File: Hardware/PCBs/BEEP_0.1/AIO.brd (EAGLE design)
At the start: 110 x 110 mm, 89 parts, among them IC1 ULN2803ASOP18, IC2 ULN2803ASOP18, U1 ATXMEGA64D3-AU, U2 TB6612FNG

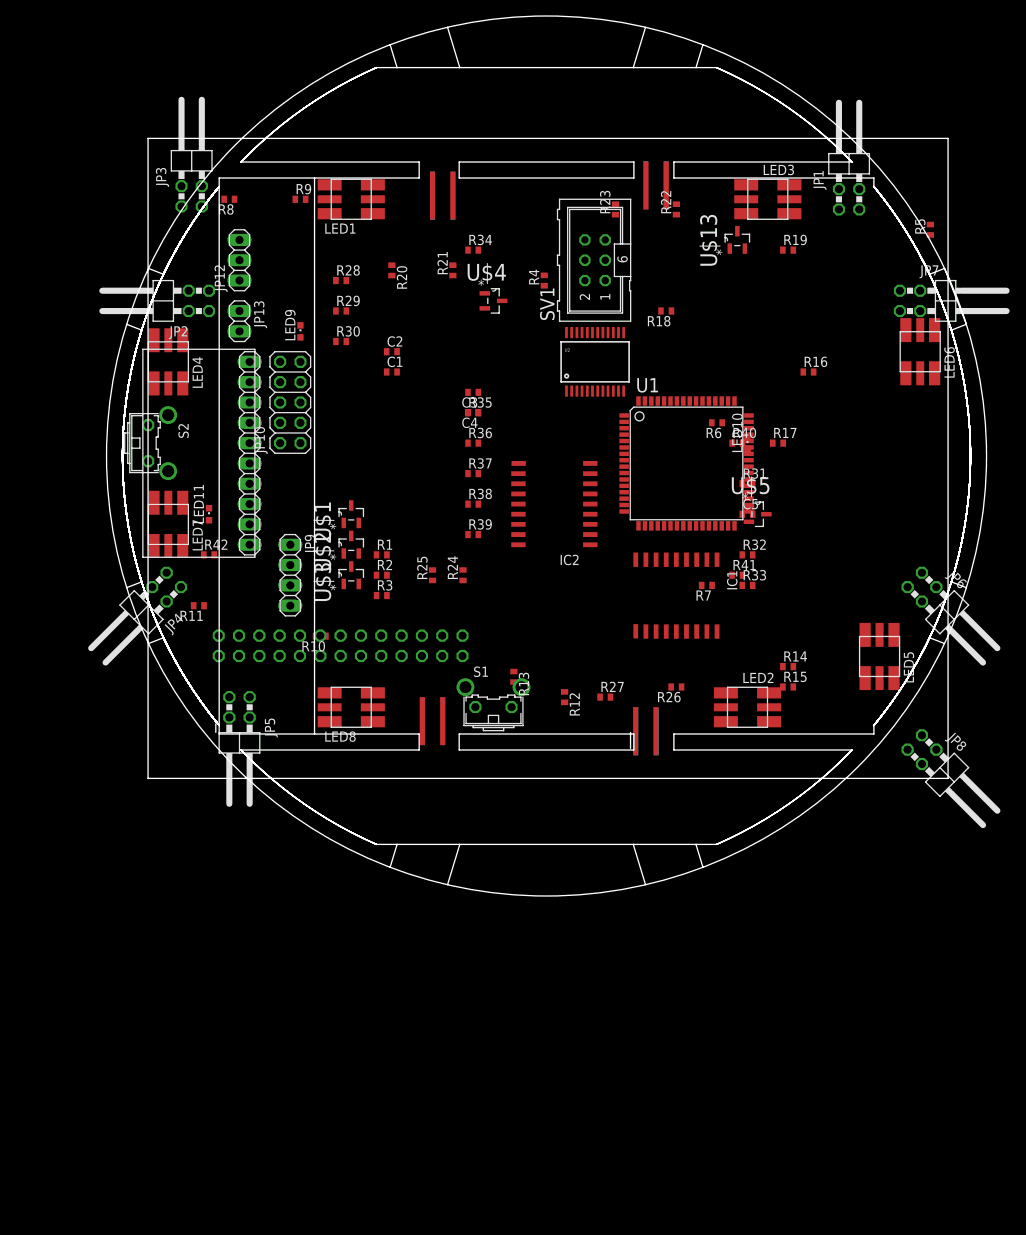
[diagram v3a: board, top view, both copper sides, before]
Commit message: enhance BEEP main pcb, rgb and ir boards
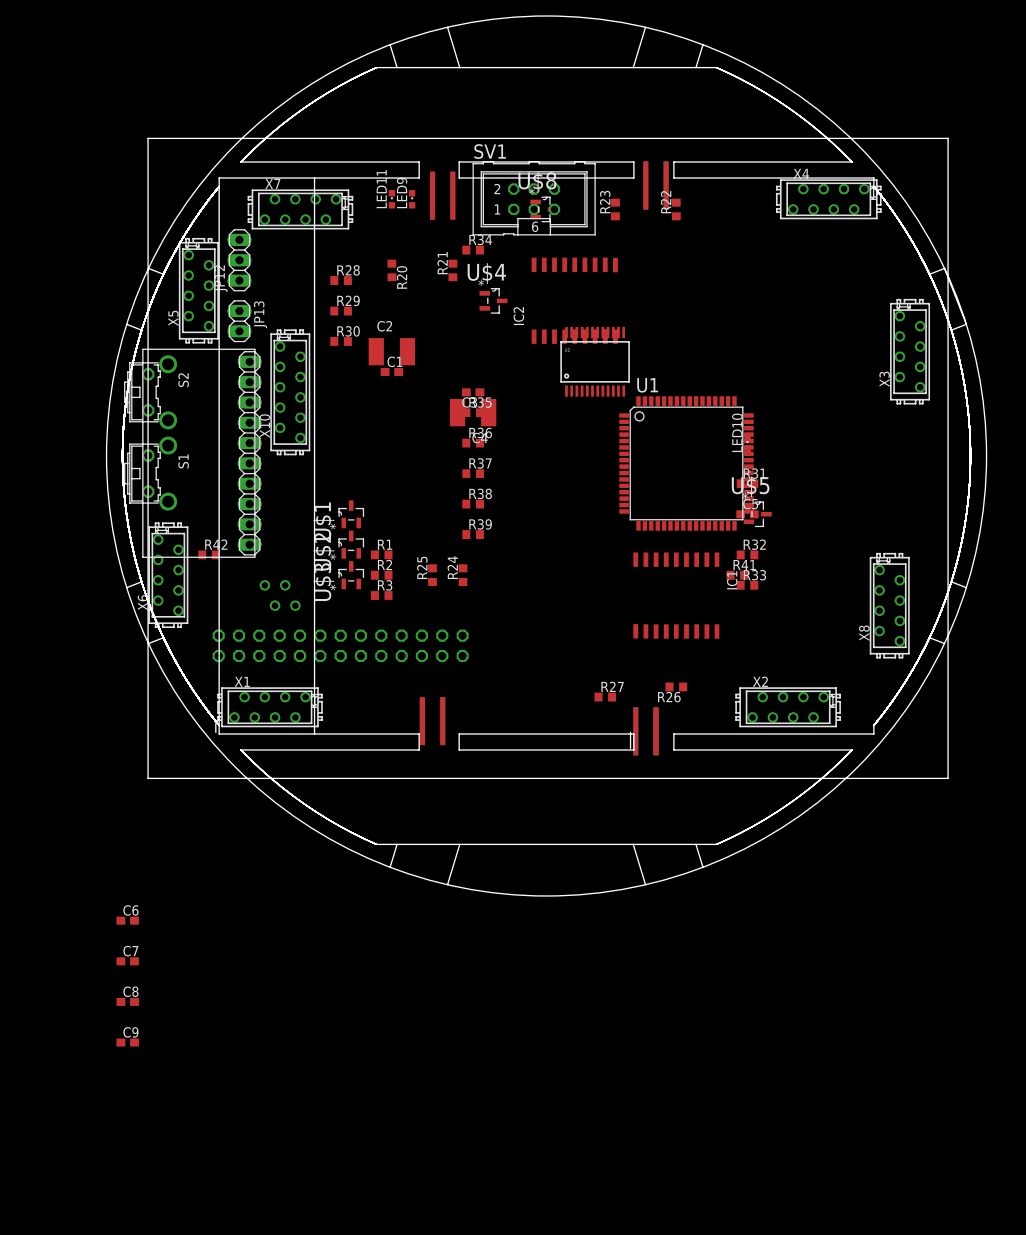
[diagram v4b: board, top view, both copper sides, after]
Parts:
- removed JP1, JP2, JP3, JP4, JP5, JP6, JP7, JP8: (no value), pinhead:2X02/90
- removed JP10: (no value), pinhead:2X05
- removed JP9: Motor_Conn, pinhead:1X04
- removed LED1, LED2, LED3, LED4, LED5, LED6, LED7, LED8: F503605050, BEEP:5050LED
- removed R10, R11, R12, R13, R14, R15, R16, R17, R18, R19, R4, R5, R6, R7, R8, R9: (no value), rcl:R0402
- removed R40: 100R, rcl:R0402
- removed U$13: DMN2075U, BEEP:SOT95P240X112-3N
- added C6, C7, C8, C9: 100nF, rcl:C0603
- added U$8: DMN2075U, BEEP:SOT95P240X112-3N
- added X1, X2, X3, X4, X5, X6, X7, X8: MICROMATCH-8, Con-amp-micromatch:MICROMATCH-8
- added X10: MICROMATCH-10, Con-amp-micromatch:MICROMATCH-10
- added X9: MICROMATCH-4, Con-amp-micromatch:MICROMATCH-4
- C1, C3, C5: device rcl:C0402 -> rcl:C0603
- C2, C4: device rcl:C0402 -> rcl:C1812
- R1, R2, R20, R21, R22, R23, R24, R25, R26, R27, R28, R29, R3, R30, R31, R32, R33, R34, R35, R36, R37, R38, R39, R41, R42: device rcl:R0402 -> rcl:R0603
- moved S1 50.4 mm to (1.27, 38.1), turned to 270 degrees
- moved LED11 45.5 mm to (30.5, 72.4)
- moved IC2 25.5 mm to (53.3, 59.7), turned to 0 degrees
- moved LED9 21.6 mm to (33.0, 72.4)
- moved SV1 10.8 mm to (48.3, 72.4), turned to 0 degrees
- moved S2 6.35 mm to (1.27, 48.3)
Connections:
- net IR_LED1 renamed IR_LED_K0
- net IR_LED2 renamed IR_LED_K1
- net IR_LED3 renamed IR_LED_K2
- net IR_LED4 renamed IR_LED_K3
- net IR_LED5 renamed IR_LED_K4
- net IR_LED6 renamed IR_LED_K5
- net IR_LED7 renamed IR_LED_K6
- net IR_LED8 renamed IR_LED_K7
- net LED1 renamed LED_K0
- net LED2 renamed LED_K1
- net LED3 renamed LED_K2
- net LED4 renamed LED_K3
- net LED5 renamed LED_K4
- net LED6 renamed LED_K5
- net LED7 renamed LED_K6
- net LED8 renamed LED_K7
- removed net ADISTANCE0: JP1.4, R5.2
- removed net ADISTANCE1: JP2.4, R7.2
- removed net ADISTANCE2: JP3.4, R9.2
- removed net ADISTANCE3: JP4.4, R11.2
- removed net ADISTANCE4: JP5.4, R13.2
- removed net ADISTANCE5: JP6.4, R15.2
- removed net ADISTANCE6: JP7.4, R17.2
- removed net ADISTANCE7: JP8.4, R19.2
- removed net IR_LED_PWM: R40.2, U$13.G
- removed net IR_PWM: R40.1
- removed net LED_A3: R37.1
- removed net N$10: IC1.15, LED4.B2, LED4.G2, LED4.R2
- removed net N$12: R10.1, R12.1, R14.1, R16.1, R18.1, R4.1, R6.1, R8.1, U$13.S
- removed net N$13: IC2.11, JP8.3
- removed net N$14: IC1.14, LED5.B2, LED5.G2, LED5.R2
- removed net N$15: IC1.13, LED6.B2, LED6.G2, LED6.R2
- removed net N$16: IC1.12, LED7.B2, LED7.G2, LED7.R2
- removed net N$17: IC1.11, LED8.B2, LED8.G2, LED8.R2
- removed net N$18: JP3.1, R8.2
- removed net N$21: JP4.1, R10.2
- removed net N$24: JP5.1, R12.2
- removed net N$27: JP6.1, R14.2
- removed net N$30: JP7.1, R16.2
- removed net N$33: LED1.R1, LED2.R1, LED3.R1, LED4.R1, LED5.R1, LED6.R1, LED7.R1, LED8.R1, R1.2
- removed net N$34: LED1.G1, LED2.G1, LED3.G1, LED4.G1, LED5.G1, LED6.G1, LED7.G1, LED8.G1, R2.2
- removed net N$35: LED1.B1, LED2.B1, LED3.B1, LED4.B1, LED5.B1, LED6.B1, LED7.B1, LED8.B1, R3.2
- removed net N$36: JP8.1, R18.2
- removed net N$4: IC1.17, LED2.B2, LED2.G2, LED2.R2
- removed net N$43: IC2.15, JP4.3
- removed net N$44: IC2.18, JP1.3
- removed net N$45: IC2.17, JP2.3
- removed net N$46: IC2.16, JP3.3
- removed net N$47: IC2.13, JP6.3
- removed net N$48: IC2.14, JP5.3
- removed net N$49: IC2.12, JP7.3
- removed net N$6: IC1.18, LED1.B2, LED1.G2, LED1.R2
- removed net N$7: IC1.16, LED3.B2, LED3.G2, LED3.R2
- removed net N$9: JP2.1, R6.2
- new net ADISTANCE_0: X4.7
- new net ADISTANCE_1: X1.7
- new net ADISTANCE_2: X2.7
- new net ADISTANCE_3: X3.7
- new net ADISTANCE_4: X5.7
- new net ADISTANCE_5: X6.7
- new net ADISTANCE_6: X7.7
- new net ADISTANCE_7: X8.7
- new net COLOR_SENSOR_PWM_LED: U$8.G
- new net IR_LED_K0_OUT: IC2.18, X4.5
- new net IR_LED_K1_OUT: IC2.17, X1.5
- new net IR_LED_K2_OUT: IC2.16, X2.5
- new net IR_LED_K3_OUT: IC2.15, X3.5
- new net IR_LED_K4_OUT: IC2.14, X5.5
- new net IR_LED_K5_OUT: IC2.13, X6.5
- new net IR_LED_K6_OUT: IC2.12, X7.5
- new net IR_LED_K7_OUT: IC2.11, X8.5
- new net LED_A0: R35.1
- new net LED_A0_OUT: R3.2, X1.1, X2.1, X3.1, X4.1, X5.1, X6.1, X7.1, X8.1
- new net LED_A1_OUT: R2.2, X1.2, X2.2, X3.2, X4.2, X5.2, X6.2, X7.2, X8.2
- new net LED_A2_OUT: R1.2, X1.3, X2.3, X3.3, X4.3, X5.3, X6.3, X7.3, X8.3
- new net LED_K0_OUT: IC1.18, X4.4
- new net LED_K1_OUT: IC1.17, X1.4
- new net LED_K2_OUT: IC1.16, X2.4
- new net LED_K3_OUT: IC1.15, X3.4
- new net LED_K4_OUT: IC1.14, X5.4
- new net LED_K5_OUT: IC1.13, X6.4
- new net LED_K6_OUT: IC1.12, X7.4
- new net LED_K7_OUT: IC1.11, X8.4
- net +3V3: now also C5.2, C6.2, C7.2, C8.2, C9.2, X10.10; no longer JP1.2, JP10.3, JP2.2, JP3.2, JP4.2, JP5.2, JP6.2, JP7.2, JP8.2
- net +5V: now also U$8.D, X1.8, X2.8, X3.8, X4.8, X5.8, X6.8, X7.8, X8.8; no longer JP10.1, U$13.D
- net COLOR_DIODE_1: now also X10.4; no longer JP10.6
- net COLOR_DIODE_2: now also X10.3; no longer JP10.4
- net COLOR_FREQ_OUT: now also X10.7; no longer JP10.7
- net COLOR_SENSOR_1: now also X10.2; no longer JP10.2
- net COLOR_SENSOR_2: now also X10.6; no longer JP10.10
- net COLOR_SENSOR_3: now also X10.5; no longer JP10.8
- net GND: now also C5.1, C6.1, C7.1, C8.1, C9.1, X1.6, X10.8, X2.6, X3.6, X4.6, X5.6, X6.6, X7.6, X8.6; no longer JP10.5, R11.1, R13.1, R15.1, R17.1, R19.1, R5.1, R7.1, R9.1
- net LED_A1: now also R36.1; no longer R35.1
- net LED_A2: now also R37.1; no longer R36.1
- net MOTOR_A_OUT1: now also X9.1; no longer JP9.4
- net MOTOR_A_OUT2: now also X9.2; no longer JP9.3
- net MOTOR_B_OUT1: now also X9.4; no longer JP9.1
- net MOTOR_B_OUT2: now also X9.3; no longer JP9.2
- net N$5: now also U$8.S, X10.9; no longer JP1.1, R4.2

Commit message: continue working on shematic for AIO BEEP started with pcb routing
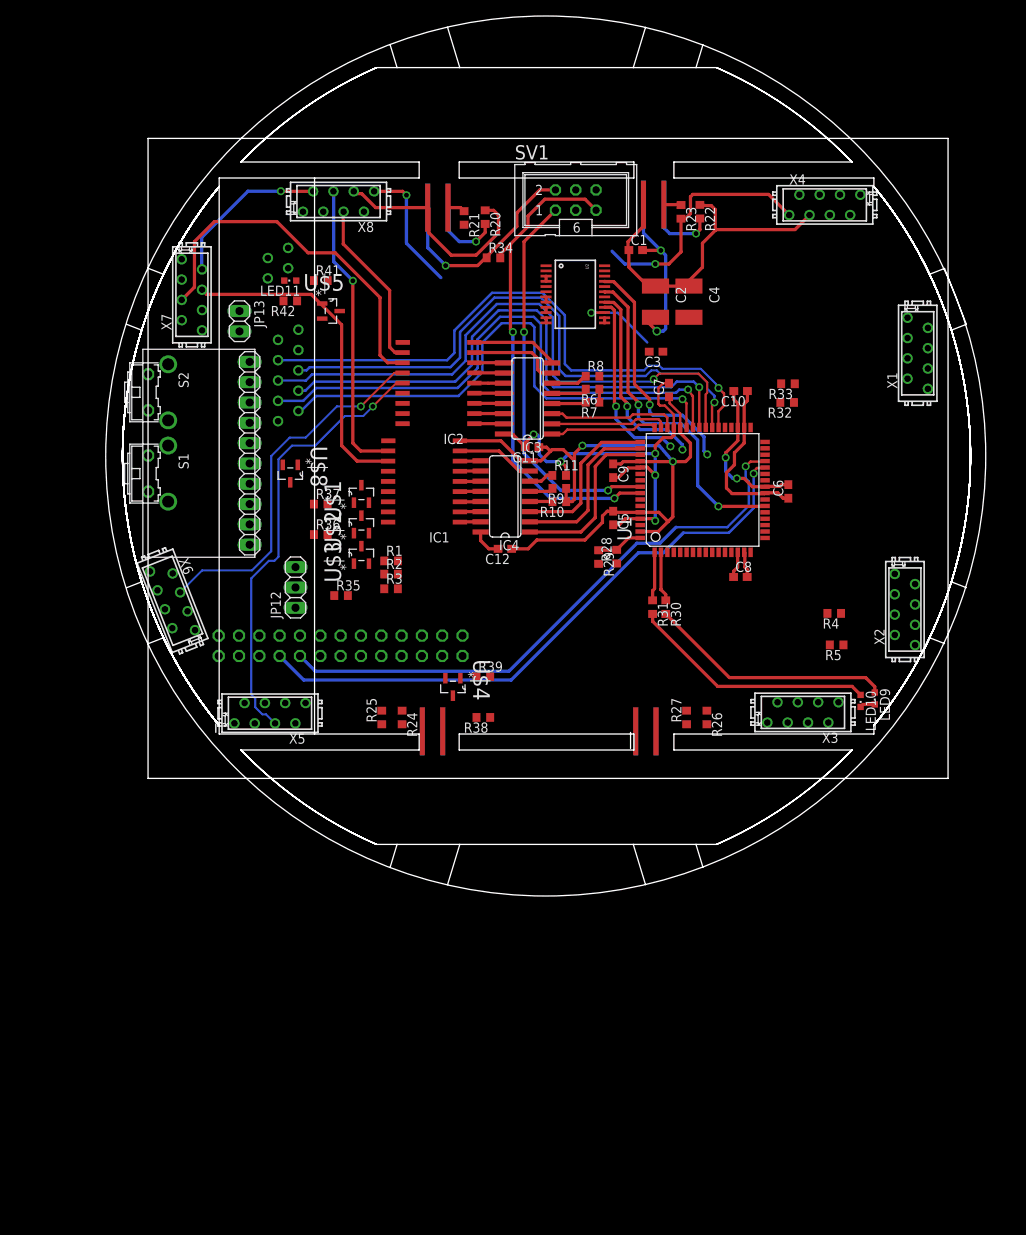
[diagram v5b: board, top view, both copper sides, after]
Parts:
- added C10, C11, C12: 100nF, rcl:C0603
- added IC3, IC4: 74HC238D, BEEP:SO16
- added R10, R11, R6, R7, R8, R9: (no value), rcl:R0603
- added R4, R5: 10K, rcl:R0603
- moved C6 98.5 mm to (80.0, 35.9), turned to 90 degrees
- moved C7 98.4 mm to (65.1, 48.5), turned to 90 degrees
- moved C9 93.8 mm to (58.1, 38.5), turned to 270 degrees
- moved C8 93.2 mm to (74.0, 25.2)
- moved X1 92.3 mm to (96.2, 53.1), turned to 90 degrees
- moved X8 85.4 mm to (23.8, 72.1), turned to 180 degrees
- moved LED9 85.1 mm to (90.8, 9.99), turned to 180 degrees
- moved R41 63.8 mm to (21.6, 62.2)
- moved U$5 59.1 mm to (22.9, 58.4)
- moved X5 53.6 mm to (15.2, 8.15), turned to 180 degrees
- moved R30 52.4 mm to (64.7, 21.4), turned to 270 degrees
- moved R28 48.8 mm to (58.6, 27.7), turned to 90 degrees
- moved U$4 48.5 mm to (38.1, 11.4), turned to 270 degrees
- moved X3 47.0 mm to (81.9, 8.25), turned to 180 degrees
- moved U$8 45.8 mm to (17.8, 38.1), turned to 270 degrees
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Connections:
- removed net AVCC: U1.61
- removed net BATT_WARN_2: LED9.A
- removed net IR_LED_K2: IC2.3
- removed net IR_LED_K3: IC2.4
- removed net IR_LED_K4: IC2.5
- removed net IR_LED_K5: IC2.6
- removed net IR_LED_K6: IC2.7
- removed net IR_LED_K7: IC2.8
- removed net LED_K0: IC1.1
- removed net LED_K1: IC1.2
- removed net LED_K2: IC1.3
- removed net LED_K3: IC1.4
- removed net LED_K4: IC1.5
- removed net LED_K5: IC1.6
- removed net LED_K6: IC1.7
- removed net LED_K7: IC1.8
- removed net PDI_CLOCK: R34.2, U1.57
- new net BATT_WARN_0: R31.1, U1.1
- new net IR_LED_MK0: IC3.1, U1.48
- new net IR_LED_MK1: IC3.2, U1.47
- new net IR_LED_MK2: IC3.3, U1.46
- new net N$10: IC2.6, IC3.10
- new net N$12: IC2.7, IC3.9
- new net N$13: IC2.8, IC3.7
- new net N$14: IC3.4, R7.2
- new net N$15: IC3.5, R6.2
- new net N$16: IC3.6, R8.1
- new net N$17: IC4.4, R10.2
- new net N$18: IC4.5, R9.2
- new net N$21: IC1.1, IC4.15
- new net N$24: IC1.2, IC4.14
- new net N$27: IC1.3, IC4.13
- new net N$28: IC1.4, IC4.12
- new net N$30: IC1.5, IC4.11
- new net N$31: IC1.6, IC4.10
- new net N$33: IC1.7, IC4.9
- new net N$34: IC1.8, IC4.7
- new net N$35: IC4.6, R11.1
- new net N$4: R4.1, R5.2, U1.62
- new net N$6: IC2.3, IC3.13
- new net N$7: IC2.4, IC3.12
- new net N$9: IC2.5, IC3.11
- new net RGB_LED_MK0: IC4.1, U1.51
- new net RGB_LED_MK1: IC4.2, U1.50
- new net RGB_LED_MK2: IC4.3, U1.49
- net +3V3: now also C10.2, C11.2, C12.2, IC3.16, IC4.16, R11.2, R5.1, R8.2, U1.61
- net ADISTANCE_0: now also U1.6
- net ADISTANCE_1: now also U1.7
- net ADISTANCE_2: now also U1.8
- net ADISTANCE_3: now also U1.9
- net ADISTANCE_4: now also U1.10
- net ADISTANCE_5: now also U1.11
- net ADISTANCE_6: now also U1.12
- net ADISTANCE_7: now also U1.13
- net BATT_VOLTAGE: now also U1.64
- net BATT_WARN_1: now also R30.1, U1.2; no longer LED10.A
- net COLOR_DIODE_1: now also U1.41
- net COLOR_DIODE_2: now also U1.42
- net COLOR_FREQ_OUT: now also U1.38
- net COLOR_SENSOR_1: now also U1.43
- net COLOR_SENSOR_2: now also U1.39
- net COLOR_SENSOR_3: now also U1.40
- net COLOR_SENSOR_PWM_LED: now also U1.19
- net GND: now also C10.1, C11.1, C12.1, IC3.8, IC4.8, LED10.C, LED9.C, R10.1, R4.2, R6.1, R7.1, R9.1, U1.63; no longer R30.2, R31.2
- net IR_LED_K0: now also IC3.15
- net IR_LED_K1: now also IC3.14
- net LED_A0: now also U1.16
- net LED_A1: now also U1.17
- net LED_A2: now also U1.18
- net MOTOR_A_IN1: now also U1.30
- net MOTOR_A_IN2: now also U1.33
- net MOTOR_A_PWM: now also U1.20
- net MOTOR_B_IN1: now also U1.31
- net MOTOR_B_IN2: now also U1.32
- net MOTOR_B_PWM: now also U1.21
- net MOTOR_STBY: now also U1.22
- net N$29: now also LED9.A, R30.2; no longer LED9.C, R30.1
- net N$32: now also LED10.A, R31.2; no longer LED10.C, R31.1
- net PDI_CLK: now also R34.2, U1.57
- net RPI_IKILL: now also U1.26
- net RPI_RX: now also U1.29
- net RPI_TX: now also U1.28
- net SCL: now also U1.37
- net SDA: now also U1.36
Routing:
- net GND: track 0.00 -> 205.2 mm, vias 0 -> 2
- net +3V3: track 0.00 -> 135.5 mm, vias 0 -> 10
- net RPI_TX: track 0.00 -> 75.6 mm, vias 0 -> 1
- net COLOR_FREQ_OUT: track 0.00 -> 75.0 mm, vias 0 -> 1
- net COLOR_SENSOR_3: track 0.00 -> 74.4 mm, vias 0 -> 1
- net RPI_RX: track 0.00 -> 73.2 mm, vias 0 -> 1
- net COLOR_SENSOR_2: track 0.00 -> 71.8 mm, vias 0 -> 1
- net COLOR_DIODE_2: track 0.00 -> 71.2 mm, vias 0 -> 1
- net COLOR_DIODE_1: track 0.00 -> 70.3 mm, vias 0 -> 1
- net COLOR_SENSOR_1: track 0.00 -> 66.7 mm, vias 0 -> 1
- net PDI_CLK: track 0.00 -> 62.1 mm, vias 0 -> 2
- net IR_LED_K4_OUT: track 0.00 -> 55.8 mm, vias 0 -> 1
- net PDI_DATA: track 0.00 -> 48.7 mm, vias 0 -> 2
- net +5V: track 0.00 -> 47.5 mm, vias 0 -> 2
- net IR_LED_K6_OUT: track 0.00 -> 46.5 mm
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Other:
- outline, holes or cut-outs redrawn
